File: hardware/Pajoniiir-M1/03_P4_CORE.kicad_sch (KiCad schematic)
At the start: 42 parts, among them U1 ESP32-P4NRW32X, U3 TLV62569DRLR

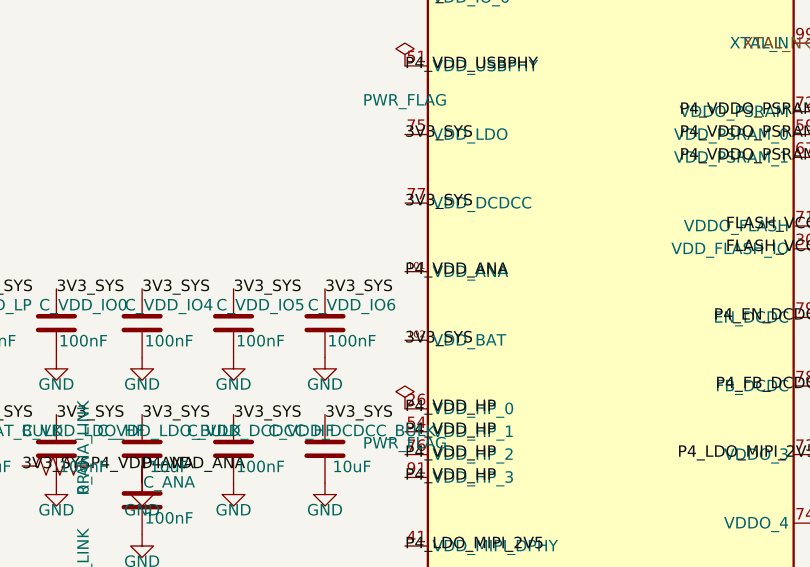
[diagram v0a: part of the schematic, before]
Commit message: hardware: declare post-link P4 analog rail source
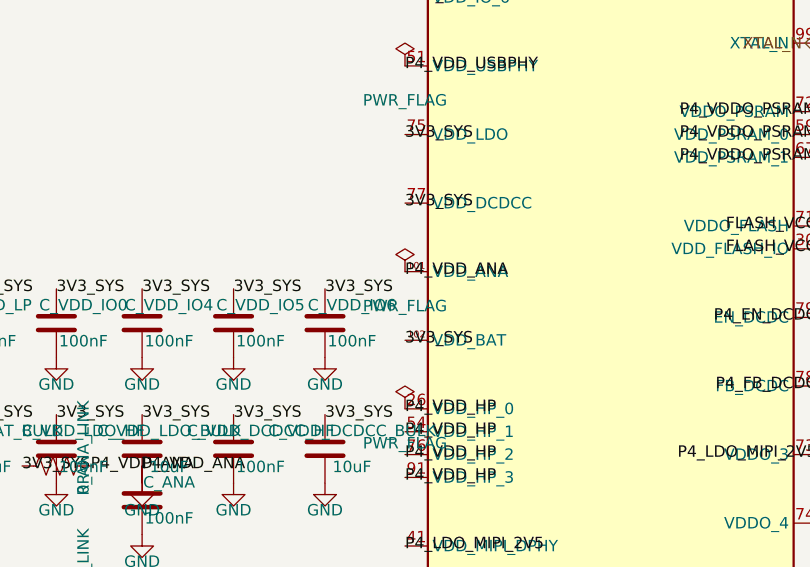
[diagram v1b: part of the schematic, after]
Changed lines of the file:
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@@
     (instances (project "Pajoniiir-M1" (path "/2c8dd352-b7b8-4d9e-8f93-5dd43be2a100/31000003-6b2a-4a3a-8c91-000000000003" (reference "#FLG0303") (unit 1))))
+  )
+  (symbol
+    (lib_id "power:PWR_FLAG")
+    (at 88.9 128.27 0)
+    (unit 1)
+    (exclude_from_sim no)
+    (in_bom yes)
+    (on_board yes)
+    (dnp no)
+    (property "Reference" "#FLG0304" (at 88.9 130.175 0) (effects (font (size 1.27 1.27)) (hide yes)))
+    (property "Value" "PWR_FLAG" (at 88.9 132.08 0) (effects (font (size 1.27 1.27))))
+    (property "Footprint" "" (at 88.9 128.27 0) (effects (font (size 1.27 1.27)) (hide yes)))
+    (property "Datasheet" "~" (at 88.9 128.27 0) (effects (font (size 1.27 1.27)) (hide yes)))
+    (property "Description" "Special symbol for telling ERC where power comes from" (at 88.9 128.27 0) (effects (font (size 1.27 1.27)) (hide yes)))
+    (pin "1")
+    (instances (project "Pajoniiir-M1" (path "/2c8dd352-b7b8-4d9e-8f93-5dd43be2a100/31000003-6b2a-4a3a-8c91-000000000003" (reference "#FLG0304") (unit 1))))
   )
   (sheet_instances (path "/" (page "4")))

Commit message: hardware: lock 2.2uH power inductors to XGL4030-222MEC
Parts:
- L_CORE: value 2.2uH -> XGL4030-222MEC / 2.2uH; footprint Inductor_SMD:L_4.0x4.0mm_TBD -> Inductor_SMD:L_Coilcraft_XxL4030
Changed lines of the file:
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@@
     (exclude_from_sim no) (in_bom yes) (on_board yes) (dnp no)
     (property "Reference" "L_CORE" (at 227.79 94.52 0) (effects (font (size 1.27 1.27))))
-    (property "Value" "2.2uH" (at 227.79 98.52 0) (effects (font (size 1.27 1.27))))
-    (property "Footprint" "Inductor_SMD:L_4.0x4.0mm_TBD" (at 224.79 96.52 0) (effects (font (size 1.27 1.27)) (hide yes)))
-    (property "Datasheet" "~" (at 224.79 96.52 0) (effects (font (size 1.27 1.27)) (hide yes)))
+    (property "Value" "XGL4030-222MEC / 2.2uH" (at 227.79 98.52 0) (effects (font (size 1.27 1.27))))
+    (property "Footprint" "Inductor_SMD:L_Coilcraft_XxL4030" (at 224.79 96.52 0) (effects (font (size 1.27 1.27)) (hide yes)))
+    (property "Datasheet" "https://www.coilcraft.com/en-us/products/power/shielded-inductors/molded-inductor/xgl/xgl4030/xgl4030-222/" (at 224.79 96.52 0) (effects (font (size 1.27 1.27)) (hide yes)))
     (pin "1") (pin "2")
     (instances (project "Pajoniiir-M1" (path "/2c8dd352-b7b8-4d9e-8f93-5dd43be2a100/31000003-6b2a-4a3a-8c91-000000000003" (reference "L_CORE") (unit 1))))

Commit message: hardware: normalize schematic reference designators
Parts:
- renumbered C_ANA to C26, C_USBPHY_1 to C27, C_USBPHY_2 to C28, C_USBPHY_3 to C29, C_VDDO_FLASH to C30, C_FLASHIO_HF to C31, C_VDDO_PSRAM to C32, C_PSRAM0_HF to C33, C_PSRAM0_LOCAL to C34, C_PSRAM1_HF to C35, C_PSRAM1_LOCAL to C36, C_MIPI_LDO_OUT to C37, C_MIPI_10N to C38, C_MIPI_100N to C39, C_CORE_IN to C40, C_CORE_OUT to C41, C_CORE_FF to C42, C_HP_BULK to C43, C_HP0 to C44, C_HP1 to C45, C_HP2 to C46, C_HP3 to C47, C_P4_3V3_BULK to C48, C_VDD_LP to C49, C_VDD_IO0 to C50, C_VDD_IO4 to C51, C_VDD_IO5 to C52, C_VDD_IO6 to C53, C_VDD_BAT_HF to C54, C_VDD_BAT_BULK to C55, C_VDD_LDO_HF to C56, C_VDD_LDO_BULK to C57, C_VDD_DCDCC_HF to C58, C_VDD_DCDCC_BULK to C59, L_CORE to L1, R_DSI_REXT to R24, R_ANA_LINK to R25, R_USBPHY_LINK to R26, R_CORE_FB_TOP to R27, R_CORE_FB_BOT to R28
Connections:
- net LCD_BL_PWM renamed LCD4_PWM

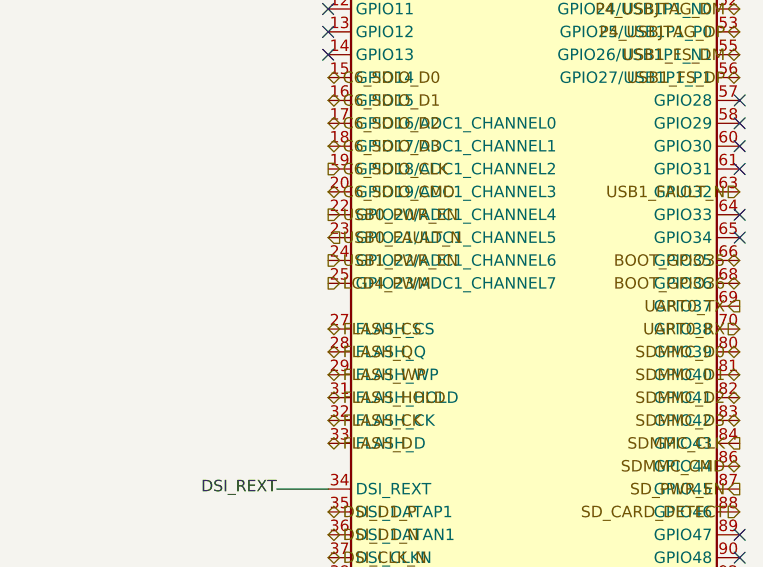
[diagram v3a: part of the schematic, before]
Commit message: hardware: constrain RefDes migration to annotation fields
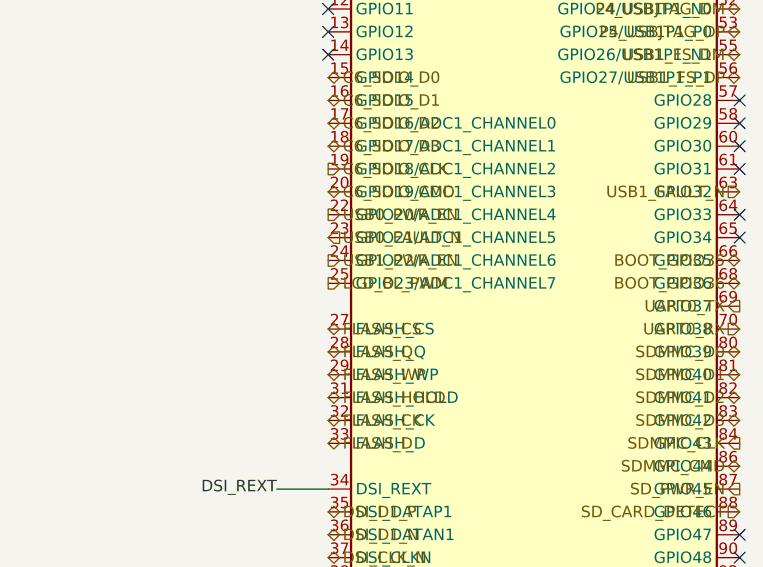
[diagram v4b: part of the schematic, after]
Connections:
- net LCD4_PWM renamed LCD_BL_PWM
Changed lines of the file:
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@@
   (hierarchical_label "USB0_FAULT_N" (shape input) (at 307.34 241.935 0) (effects (font (size 1.27 1.27))))
   (hierarchical_label "USB1_PWR_EN" (shape output) (at 307.34 244.475 0) (effects (font (size 1.27 1.27))))
-  (hierarchical_label "LCD4_PWM" (shape output) (at 307.34 247.015 0) (effects (font (size 1.27 1.27))))
+  (hierarchical_label "LCD_BL_PWM" (shape output) (at 307.34 247.015 0) (effects (font (size 1.27 1.27))))
   (hierarchical_label "FLASH_CS" (shape bidirectional) (at 307.34 252.095 0) (effects (font (size 1.27 1.27))))
   (hierarchical_label "FLASH_Q" (shape bidirectional) (at 307.34 254.635 0) (effects (font (size 1.27 1.27))))
